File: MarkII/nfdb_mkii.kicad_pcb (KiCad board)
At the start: 2 copper layers, 115.7 x 33.5 mm, 43 parts, among them J1 TYPE-C-31-M-12, J2 TYPE-C-31-M-12, J3 JST_EH_S4B-EH_1x04_P2.50mm_Ho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, J4 JST_PH_S5B-PH-SM4-TB_1x05-1MP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, J5 TYPE-C-31-M-12, J6 TYPE-C-31-M-12, U1 USBLC6-2SC6, U2 USBLC6-2SC6

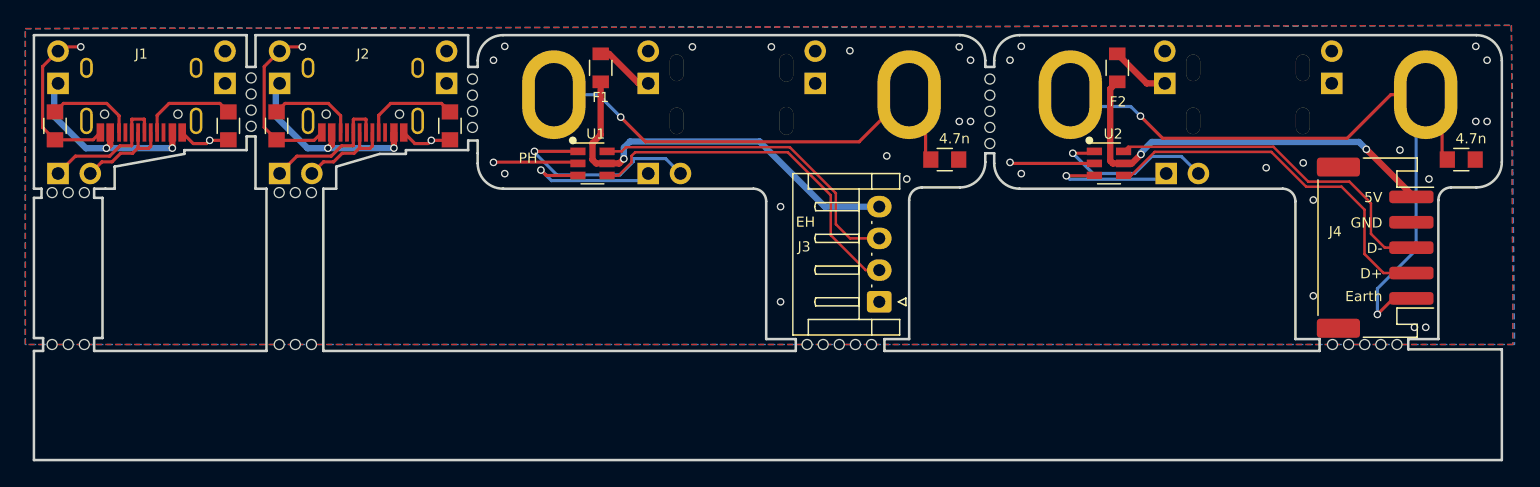
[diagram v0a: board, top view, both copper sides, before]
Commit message: Fixed mkii R2 ground traces
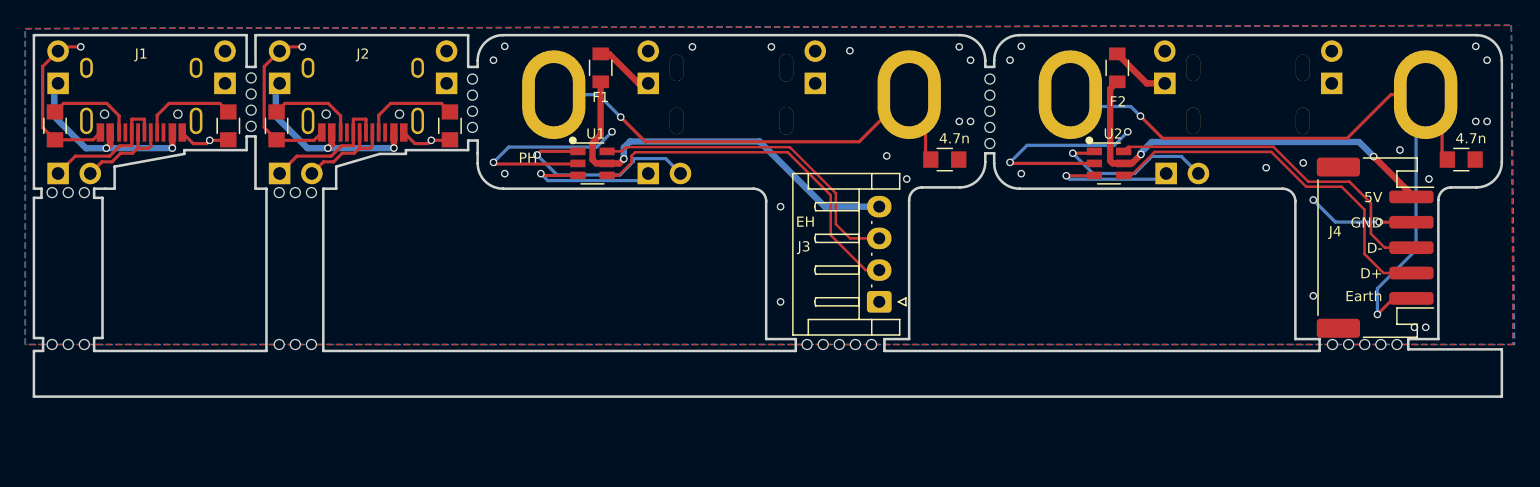
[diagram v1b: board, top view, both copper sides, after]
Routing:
- net GND: track 48.9 -> 78.1 mm, vias 35 -> 38
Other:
- board size 115.7 x 33.5 mm -> 115.7 x 28.5 mm
- board text added: "Rev 1.2 RF 1"
- board text added: "Rev 1.2 RF 2"
- board text removed: "Rev 1.1 RF 1"
- board text removed: "Rev 1.1 RF 2"
